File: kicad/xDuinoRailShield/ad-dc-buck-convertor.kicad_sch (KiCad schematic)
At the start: 14 parts, among them U1 TPS5430DDA

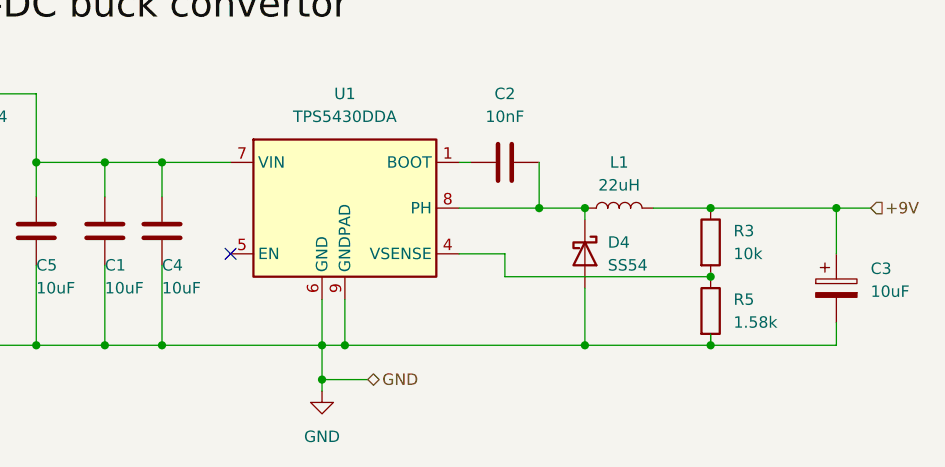
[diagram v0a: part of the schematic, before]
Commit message: Add more extractor
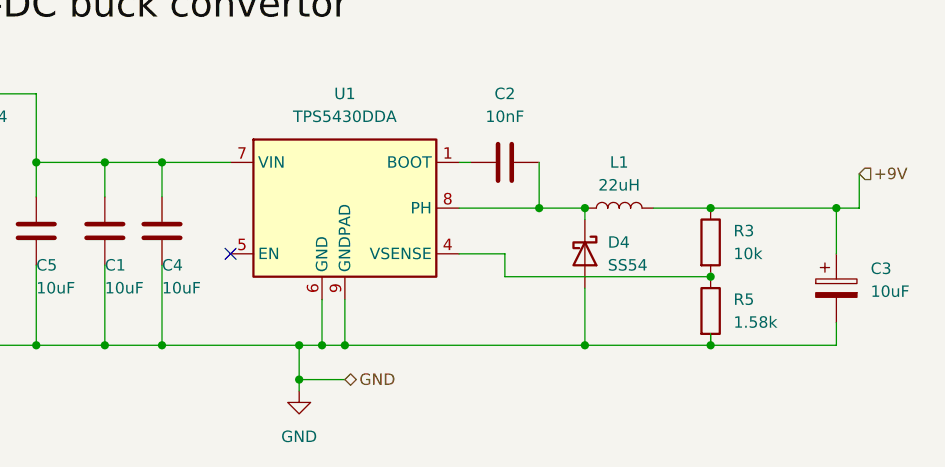
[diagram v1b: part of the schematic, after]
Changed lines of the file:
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@@
 (kicad_sch (version 20230121) (generator eeschema)
   (paper "A4")
+  (junction (at 104.14 63.5) (diameter 0) (color 0 0 0 0)
+  )
   (junction (at 109.22 63.5) (diameter 0) (color 0 0 0 0)
   )
@@
   (junction (at 149.86 48.26) (diameter 0) (color 0 0 0 0)
   )
-  (junction (at 106.68 67.31) (diameter 0) (color 0 0 0 0)
+  (junction (at 104.14 67.31) (diameter 0) (color 0 0 0 0)
   )
   (junction (at 55.88 43.18) (diameter 0) (color 0 0 0 0)
   )
+  (junction (at 163.83 48.26) (diameter 0) (color 0 0 0 0)
+  )
   (junction (at 149.86 55.88) (diameter 0) (color 0 0 0 0)
-  )
-  (junction (at 163.83 48.26) (diameter 0) (color 0 0 0 0)
   )
   (junction (at 106.68 63.5) (diameter 0) (color 0 0 0 0)
@@
     (stroke (width 0) (type default))
   )
-  (wire (pts (xy 106.68 68.58) (xy 106.68 67.31))
+  (wire (pts (xy 104.14 68.58) (xy 104.14 67.31))
     (stroke (width 0) (type default))
   )
@@
     (stroke (width 0) (type default))
   )
+  (wire (pts (xy 104.14 63.5) (xy 106.68 63.5))
+    (stroke (width 0) (type default))
+  )
   (wire (pts (xy 109.22 63.5) (xy 135.89 63.5))
     (stroke (width 0) (type default))
@@
     (stroke (width 0) (type default))
   )
+  (wire (pts (xy 166.37 48.26) (xy 163.83 48.26))
+    (stroke (width 0) (type default))
+  )
   (wire (pts (xy 163.83 48.26) (xy 163.83 53.34))
     (stroke (width 0) (type default))
@@
     (stroke (width 0) (type default))
   )
-  (wire (pts (xy 88.9 63.5) (xy 106.68 63.5))
-    (stroke (width 0) (type default))
-  )
-  (wire (pts (xy 106.68 67.31) (xy 106.68 63.5))
+  (wire (pts (xy 88.9 63.5) (xy 104.14 63.5))
+    (stroke (width 0) (type default))
+  )
+  (wire (pts (xy 104.14 67.31) (xy 104.14 63.5))
     (stroke (width 0) (type default))
   )
@@
     (stroke (width 0) (type default))
   )
-  (wire (pts (xy 111.76 67.31) (xy 106.68 67.31))
+  (wire (pts (xy 109.22 67.31) (xy 104.14 67.31))
     (stroke (width 0) (type default))
   )
@@
     (stroke (width 0) (type default))
   )
-  (wire (pts (xy 163.83 48.26) (xy 167.64 48.26))
+  (wire (pts (xy 166.37 48.26) (xy 166.37 44.45))
     (stroke (width 0) (type default))
   )
@@
     (effects (font (size 3 3)) (justify left bottom))
   )
-  (hierarchical_label "+9V" (shape input) (at 167.64 48.26 0) (fields_autoplaced)
+  (hierarchical_label "+9V" (shape input) (at 166.37 44.45 0) (fields_autoplaced)
     (effects (font (size 1.27 1.27)) (justify left))
   )
@@
     (effects (font (size 1.27 1.27)) (justify right))
   )
-  (hierarchical_label "GND" (shape bidirectional) (at 111.76 67.31 0) (fields_autoplaced)
+  (hierarchical_label "GND" (shape bidirectional) (at 109.22 67.31 0) (fields_autoplaced)
     (effects (font (size 1.27 1.27)) (justify left))
   )
@@
     )
   )
-  (symbol (lib_id "power:GND") (at 106.68 68.58 0) (unit 1)
+  (symbol (lib_id "power:GND") (at 104.14 68.58 0) (unit 1)
     (in_bom yes) (on_board yes) (dnp no) (fields_autoplaced)
-    (property "Reference" "#PWR05" (at 106.68 74.93 0)
-      (effects (font (size 1.27 1.27)) hide)
-    )
-    (property "Value" "GND" (at 106.68 73.66 0)
+    (property "Reference" "#PWR05" (at 104.14 74.93 0)
+      (effects (font (size 1.27 1.27)) hide)
+    )
+    (property "Value" "GND" (at 104.14 73.66 0)
       (effects (font (size 1.27 1.27)))
     )
-    (property "Footprint" "" (at 106.68 68.58 0)
-      (effects (font (size 1.27 1.27)) hide)
-    )
-    (property "Datasheet" "" (at 106.68 68.58 0)
-      (effects (font (size 1.27 1.27)) hide)
-    )
+    (property "Footprint" "" (at 104.14 68.58 0)
+      (effects (font (size 1.27 1.27)) hide)
+    )
+    (property "Datasheet" "" (at 104.14 68.58 0)
+      (effects (font (size 1.27 1.27)) hide)
+    )

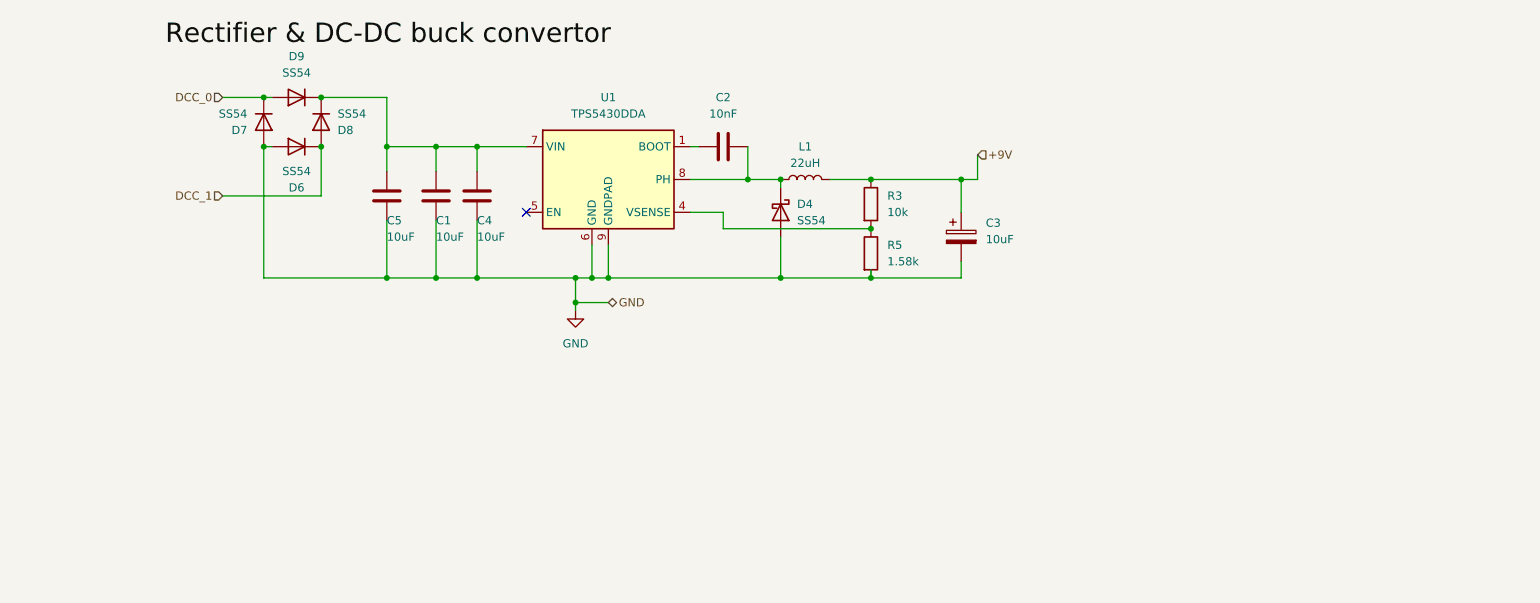
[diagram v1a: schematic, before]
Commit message: More options, more Partnumbers
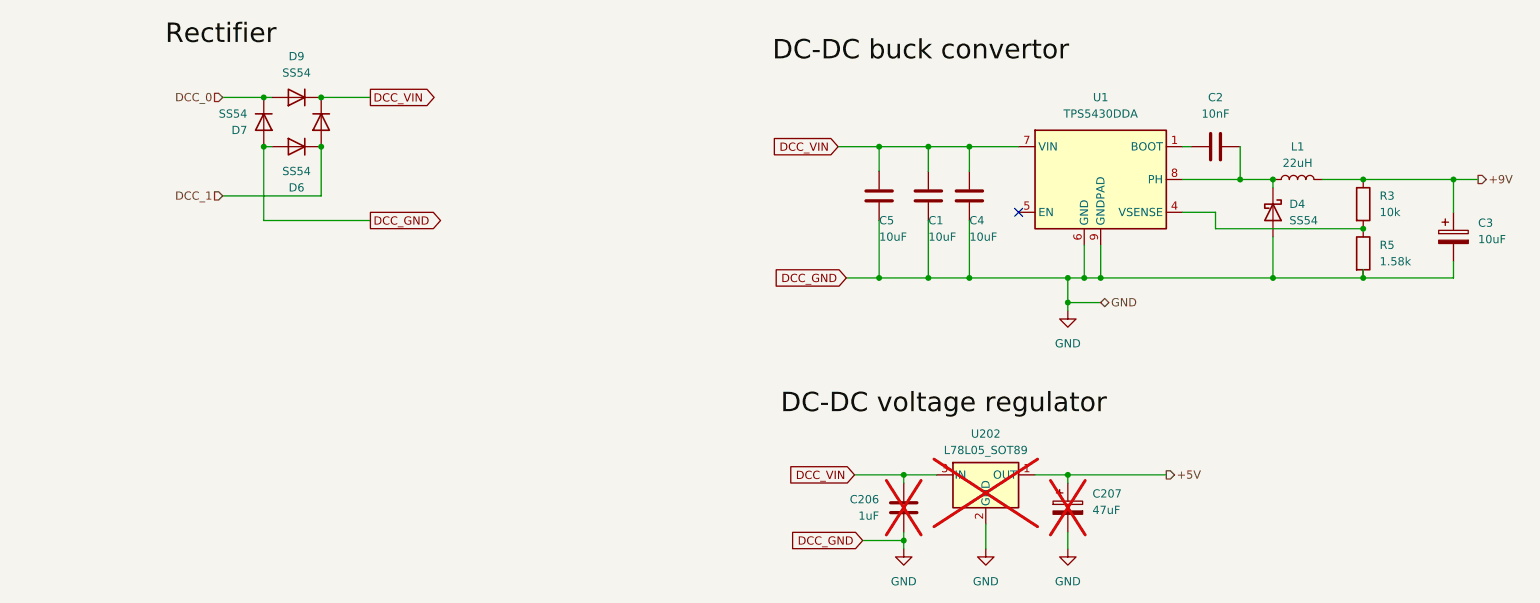
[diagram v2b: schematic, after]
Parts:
- added C206: 1uF, symbol Device:C
- added C207: 47uF, symbol Device:C_Polarized
- added U202: L78L05_SOT89, Package_TO_SOT_SMD:SOT-89-3, symbol Regulator_Linear:L78L05_SOT89
- C3: footprint Capacitor_SMD:C_0805_2012Metric -> Capacitor_SMD:C_1206_3216Metric
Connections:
- net GND: now also C206.2, C207.2, U202.2 (GND)
- net DCC_VIN: now reaches C1.1, C4.1, C5.1, D8.1 (K), D9.1 (K), U1.7 (VIN)
- net DCC_VIN: now also C206.1, U202.3 (IN)
- new net +5V: C207.1, U202.1 (OUT)

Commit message: Another iteration on the layout
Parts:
- renumbered C5 to C201, C1 to C202, C4 to C203, C2 to C204, C3 to C205, D7 to D201, D9 to D202, D6 to D203, D8 to D204, D4 to D205, L1 to L201, R3 to R201, R5 to R202, U1 to U201

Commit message: xXiaoCentralMini
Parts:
- C1: renamed from C201; now not fitted
- C2: renamed from C206; now fitted
- C3: renamed from C202; now not fitted
- C4: renamed from C203; now not fitted
- C5: renamed from C207; now fitted
- C6: renamed from C204; now not fitted
- C7: renamed from C205; now not fitted
- D5: renamed from D205; now not fitted
- L1: renamed from L201; now not fitted
- R1: renamed from R201; footprint Resistor_SMD:R_0805_2012Metric_Pad1.20x1.40mm_HandSolder -> Resistor_SMD:R_0603_1608Metric_Pad0.98x0.95mm_HandSolder; now not fitted
- R2: renamed from R202; footprint Resistor_SMD:R_0805_2012Metric_Pad1.20x1.40mm_HandSolder -> Resistor_SMD:R_0603_1608Metric_Pad0.98x0.95mm_HandSolder; now not fitted
- U1: renamed from U202; now fitted
- U2: renamed from U201; now not fitted
- renumbered D201 to D1, D202 to D2, D203 to D3, D204 to D4

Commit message: More busses added
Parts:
- R802: renamed from R2; value 1.58k -> 2k
- renumbered C1 to C801, C2 to C802, C3 to C803, C4 to C804, C5 to C805, C6 to C806, C7 to C807, D1 to D801, D2 to D802, D3 to D803, D4 to D804, D5 to D805, L1 to L801, R1 to R801, U1 to U801, U2 to U802
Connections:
- net +9V renamed +7V2
- net DCC_0 renamed DCC0
- net DCC_1 renamed DCC1

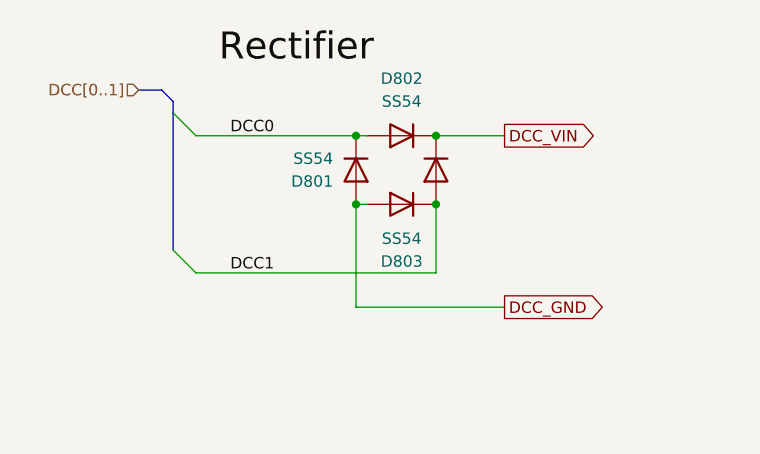
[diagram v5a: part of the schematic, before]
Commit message: Draft of loco decoder
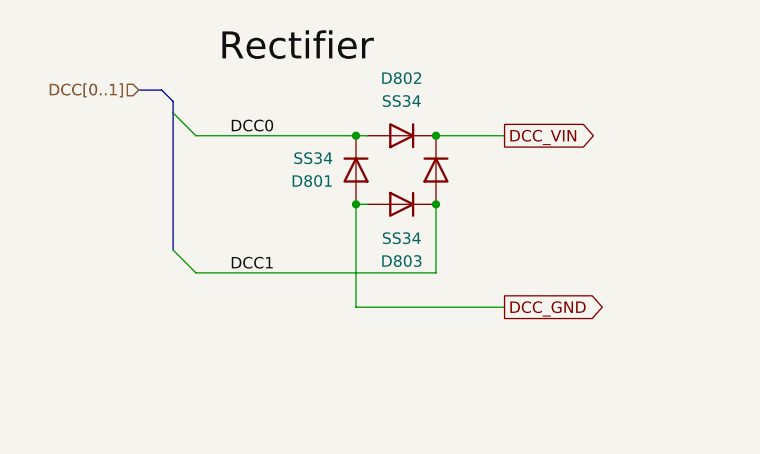
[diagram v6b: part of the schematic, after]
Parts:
- C802: footprint (none) -> Capacitor_SMD:C_0805_2012Metric_Pad1.18x1.45mm_HandSolder; LCSC (none) -> C28323
- C805: footprint (none) -> Capacitor_SMD:C_0805_2012Metric_Pad1.18x1.45mm_HandSolder; LCSC (none) -> C16780
- D801, D802, D803, D804: value SS54 -> SS34; LCSC C22452 -> C8678
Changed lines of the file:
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@@
 			)
 		)
-		(property "Footprint" ""
+		(property "Footprint" "Capacitor_SMD:C_0805_2012Metric_Pad1.18x1.45mm_HandSolder"
 			(at 181.3052 102.87 0)
 			(effects
@@
 		)
 		(property "Description" ""
+			(at 180.34 99.06 0)
+			(effects
+				(font
+					(size 1.27 1.27)
+				)
+				(hide yes)
+			)
+		)
+		(property "Field-1" ""
+			(at 180.34 99.06 0)
+			(effects
+				(font
+					(size 1.27 1.27)
+				)
+				(hide yes)
+			)
+		)
+		(property "LCSC" "C16780"
 			(at 180.34 99.06 0)
 			(effects
@@
 		)
 		(property "LCSC" "C22452"
+			(at 212.09 53.34 0)
+			(effects
+				(font
+					(size 1.27 1.27)
+				)
+				(hide yes)
+			)
+		)
+		(property "Field-1" ""
 			(at 212.09 53.34 0)
 			(effects
@@
 			)
 		)
+		(property "Field-1" ""
+			(at 226.06 52.07 0)
+			(effects
+				(font
+					(size 1.27 1.27)
+				)
+				(hide yes)
+			)
+		)
 		(pin "1"
 		)
@@
 			)
 		)
+		(property "Field-1" ""
+			(at 158.75 50.8 0)
+			(effects
+				(font
+					(size 1.27 1.27)
+				)
+				(hide yes)
+			)
+		)
 		(pin "1"
 		)
@@
 			)
 		)
+		(property "Field-1" ""
+			(at 203.2 43.18 0)
+			(effects
+				(font
+					(size 1.27 1.27)
+				)
+				(hide yes)
+			)
+		)
 		(pin "1"
 		)
@@
 			)
 		)
-		(property "Value" "SS54"
+		(property "Value" "SS34"
 			(at 53.34 38.1 90)
 			(effects
@@
 			)
 		)
-		(property "LCSC" "C22452"
+		(property "LCSC" "C8678"
+			(at 55.88 39.37 0)
+			(effects
+				(font
+					(size 1.27 1.27)
+				)
+				(hide yes)
+			)
+		)
+		(property "Field-1" ""
 			(at 55.88 39.37 0)
 			(effects
@@
 			)
 		)
-		(property "Value" "SS54"
+		(property "Value" "SS34"
 			(at 60.96 31.75 0)
 			(effects
@@
 			)
 		)
-		(property "LCSC" "C22452"
+		(property "LCSC" "C8678"
+			(at 60.96 35.56 0)
+			(effects
+				(font
+					(size 1.27 1.27)
+				)
+				(hide yes)
+			)
+		)
+		(property "Field-1" ""
 			(at 60.96 35.56 0)
 			(effects
@@
 			)
 		)
+		(property "Field-1" ""
+			(at 185.42 48.26 0)
+			(effects
+				(font
+					(size 1.27 1.27)
+				)
+				(hide yes)
+			)
+		)
 		(pin "1"
 		)
@@
 			)
 		)
+		(property "Field-1" ""
+			(at 215.9 48.26 0)
+			(effects
+				(font
+					(size 1.27 1.27)
+				)
+				(hide yes)
+			)
+		)
 		(pin "1"
 		)
@@
 			)
 		)
+		(property "Field-1" ""
+			(at 167.64 93.98 0)
+			(effects
+				(font
+					(size 1.27 1.27)
+				)
+				(hide yes)
+			)
+		)
 		(pin "1"
 		)
@@
 			)
 		)
-		(property "Value" "SS54"
+		(property "Value" "SS34"
 			(at 60.96 46.99 0)
 			(effects
@@
 			)
 		)
-		(property "LCSC" "C22452"
+		(property "LCSC" "C8678"
+			(at 60.96 43.18 0)
+			(effects
+				(font
+					(size 1.27 1.27)
+				)
+				(hide yes)
+			)
+		)
+		(property "Field-1" ""
 			(at 60.96 43.18 0)
 			(effects
@@
 			)
 		)
-		(property "Footprint" ""
+		(property "Footprint" "Capacitor_SMD:C_0805_2012Metric_Pad1.18x1.45mm_HandSolder"
 			(at 153.9748 102.87 0)
 			(effects
@@
 		)
 		(property "Description" ""
+			(at 154.94 99.06 0)
+			(effects
+				(font
+					(size 1.27 1.27)
+				)
+				(hide yes)
+			)
+		)
+		(property "Field-1" ""
+			(at 154.94 99.06 0)
+			(effects
+				(font
+					(size 1.27 1.27)
+				)
+				(hide yes)
+			)
+		)
+		(property "LCSC" "C28323"
 			(at 154.94 99.06 0)
 			(effects
@@
 			)
 		)
+		(property "Field-1" ""
+			(at 226.06 59.69 0)
+			(effects
+				(font
+					(size 1.27 1.27)
+				)
+				(hide yes)
+			)
+		)
 		(pin "1"
 		)
@@
 		)
 		(property "LCSC" "C13585"
+			(at 165.1 50.8 0)
+			(effects
+				(font
+					(size 1.27 1.27)
+				)
+				(hide yes)
+			)
+		)
+		(property "Field-1" ""
 			(at 165.1 50.8 0)
 			(effects
@@
 			)
 		)
+		(property "Field-1" ""
+			(at 240.03 57.15 0)
+			(effects
+				(font
+					(size 1.27 1.27)
+				)
+				(hide yes)
+			)
+		)
 		(pin "1"
 		)
@@
 			)
 		)
-		(property "Value" "SS54"
+		(property "Value" "SS34"
 			(at 67.31 38.1 90)
 			(effects
@@
 			)
 		)
-		(property "LCSC" "C22452"
+		(property "LCSC" "C8678"
+			(at 64.77 39.37 0)
+			(effects
+				(font
+					(size 1.27 1.27)
+				)
+				(hide yes)
+			)
+		)
+		(property "Field-1" ""
 			(at 64.77 39.37 0)
 			(effects
@@
 			(at 151.13 50.8 0)
 			(effects
+				(font
+					(size 1.27 1.27)
+				)
+				(hide yes)
+			)
+		)
+		(property "Field-1" ""
+			(at 151.13 50.8 0)
+			(effects

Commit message: A lot of fixes
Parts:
- R701: renamed from R801; footprint Resistor_SMD:R_0603_1608Metric_Pad0.98x0.95mm_HandSolder -> Resistor_SMD:R_0805_2012Metric_Pad1.20x1.40mm_HandSolder
- R702: renamed from R802; footprint Resistor_SMD:R_0603_1608Metric_Pad0.98x0.95mm_HandSolder -> Resistor_SMD:R_0805_2012Metric_Pad1.20x1.40mm_HandSolder
- renumbered C801 to C701, C802 to C702, C803 to C703, C804 to C704, C805 to C705, C806 to C706, C807 to C707, D801 to D701, D802 to D702, D803 to D703, D804 to D704, D805 to D705, L801 to L701, U801 to U701, U802 to U702
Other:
- note added: "Bridge Rectifier"
- note added: "DC-DC buck convertor"
- note added: "DC-DC voltage regulator"
- moved on the sheet: D701, D702, D703

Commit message: Refactoring & Sound
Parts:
- C702, C705: footprint Capacitor_SMD:C_0805_2012Metric_Pad1.18x1.45mm_HandSolder -> Capacitor_SMD:C_0402_1005Metric_Pad0.74x0.62mm_HandSolder
- D701, D702, D703, D704: value SS34 -> 1N5819WS; footprint Diode_SMD:D_SMA -> Diode_SMD:D_SOD-323
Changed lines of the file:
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@@
 			)
 		)
-		(property "Footprint" "Capacitor_SMD:C_0805_2012Metric_Pad1.18x1.45mm_HandSolder"
+		(property "Footprint" "Capacitor_SMD:C_0402_1005Metric_Pad0.74x0.62mm_HandSolder"
 			(at 181.3052 102.87 0)
 			(effects
@@
 			)
 		)
-		(property "Value" "SS34"
+		(property "Value" "1N5819WS"
 			(at 43.18 52.07 90)
 			(effects
@@
 			)
 		)
-		(property "Footprint" "Diode_SMD:D_SMA"
+		(property "Footprint" "Diode_SMD:D_SOD-323"
 			(at 45.72 53.34 0)
 			(effects
@@
 			)
 		)
-		(property "Value" "SS34"
+		(property "Value" "1N5819WS"
 			(at 50.8 45.72 0)
 			(effects
@@
 			)
 		)
-		(property "Footprint" "Diode_SMD:D_SMA"
+		(property "Footprint" "Diode_SMD:D_SOD-323"
 			(at 50.8 49.53 0)
 			(effects
@@
 			)
 		)
-		(property "Value" "SS34"
+		(property "Value" "1N5819WS"
 			(at 50.8 60.96 0)
 			(effects
@@
 			)
 		)
-		(property "Footprint" "Diode_SMD:D_SMA"
+		(property "Footprint" "Diode_SMD:D_SOD-323"
 			(at 50.8 57.15 0)
 			(effects
@@
 			)
 		)
-		(property "Footprint" "Capacitor_SMD:C_0805_2012Metric_Pad1.18x1.45mm_HandSolder"
+		(property "Footprint" "Capacitor_SMD:C_0402_1005Metric_Pad0.74x0.62mm_HandSolder"
 			(at 153.9748 102.87 0)
 			(effects
@@
 			)
 		)
-		(property "Value" "SS34"
+		(property "Value" "1N5819WS"
 			(at 57.15 52.07 90)
 			(effects
@@
 			)
 		)
-		(property "Footprint" "Diode_SMD:D_SMA"
+		(property "Footprint" "Diode_SMD:D_SOD-323"
 			(at 54.61 53.34 0)
 			(effects
